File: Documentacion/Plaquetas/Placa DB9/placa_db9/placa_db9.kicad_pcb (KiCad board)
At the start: 2 copper layers, 30 x 16.5 mm, 2 parts, among them J1 Conn_01x09, J2 DB9_Female_MountingHoles

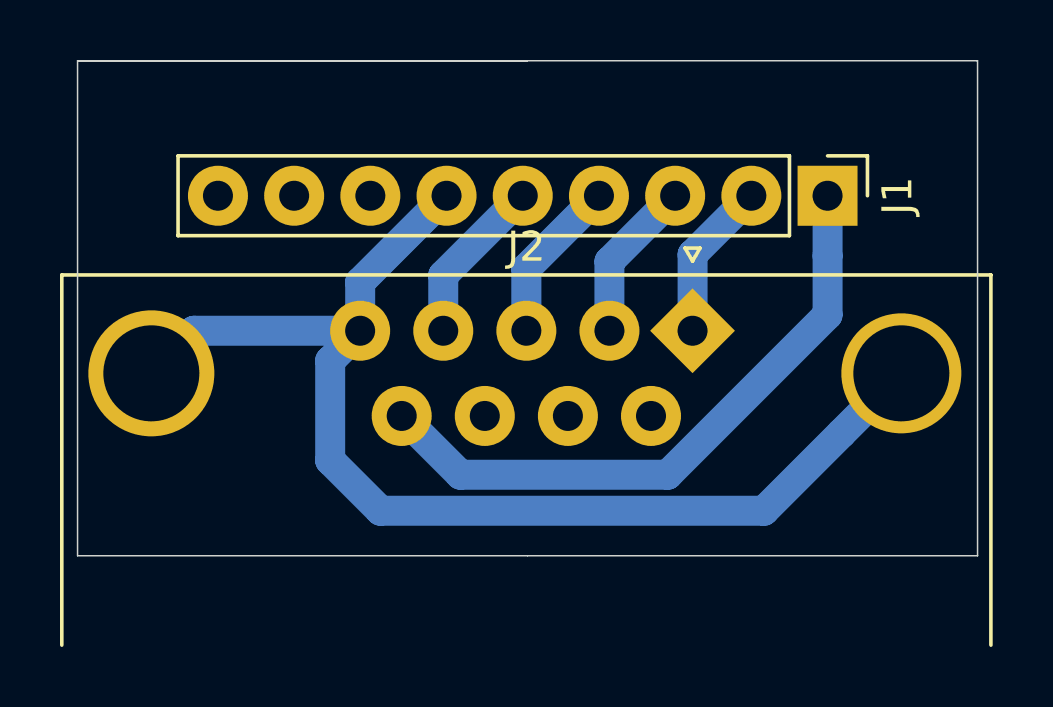
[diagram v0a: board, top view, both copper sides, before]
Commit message: DB9 board with bigger pads
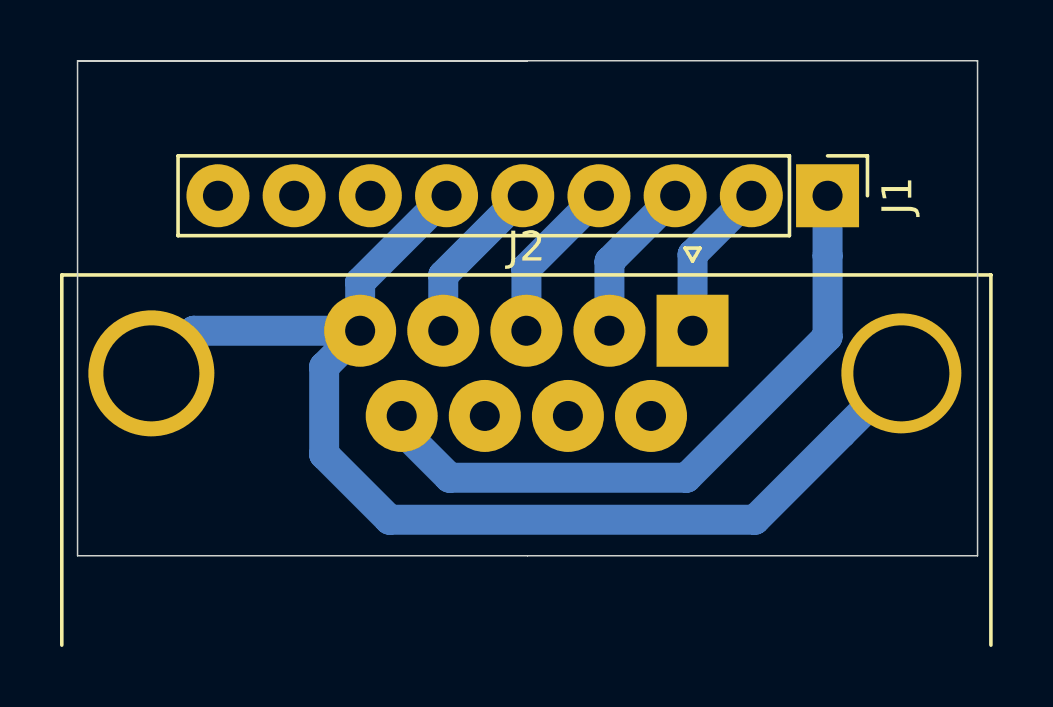
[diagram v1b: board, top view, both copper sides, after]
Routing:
- net /fan_1: track 21.2 -> 22.0 mm
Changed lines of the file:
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@@
     (thickness 1.6)
     (drawings 14)
-    (tracks 23)
+    (tracks 24)
     (zones 0)
     (modules 2)
@@
   )
   (setup
-    (last_trace_width 0.25)
+    (last_trace_width 1)
     (user_trace_width 0.7)
     (user_trace_width 1)
@@
     (descr "Through hole straight pin header, 1x09, 2.54mm pitch, single row")
     (tags "Through hole pin header THT 1x09 2.54mm single row")
-    (fp_text reference J1 (at 0 -2.33 270) (layer F.SilkS)
+    (fp_text reference J1 (at 0 -2.33 90) (layer F.SilkS)
       (effects (font (size 1 1) (thickness 0.15)))
     )
@@
       (effects (font (size 1 1) (thickness 0.15)))
     )
-    (pad 1 thru_hole rect (at 0 0 270) (size 2 2) (drill 1) (layers *.Cu *.Mask)
+    (pad 1 thru_hole rect (at 0 0 270) (size 2.1 2.1) (drill 1) (layers *.Cu *.Mask)
       (net 7 /fan_1))
-    (pad 2 thru_hole oval (at 0 2.54 270) (size 2 2) (drill 1) (layers *.Cu *.Mask)
+    (pad 2 thru_hole circle (at 0 2.54 270) (size 2.1 2.1) (drill 1) (layers *.Cu *.Mask)
       (net 8 /term_pelt_1))
-    (pad 3 thru_hole circle (at 0 5.08 270) (size 2 2) (drill 1) (layers *.Cu *.Mask)
+    (pad 3 thru_hole circle (at 0 5.08 270) (size 2.1 2.1) (drill 1) (layers *.Cu *.Mask)
       (net 9 /term_pelt_2))
-    (pad 4 thru_hole circle (at 0 7.62 270) (size 2 2) (drill 1) (layers *.Cu *.Mask)
+    (pad 4 thru_hole circle (at 0 7.62 270) (size 2.1 2.1) (drill 1) (layers *.Cu *.Mask)
       (net 10 /term_disip_1))
-    (pad 5 thru_hole circle (at 0 10.16 270) (size 2 2) (drill 1) (layers *.Cu *.Mask)
+    (pad 5 thru_hole circle (at 0 10.16 270) (size 2.1 2.1) (drill 1) (layers *.Cu *.Mask)
       (net 11 /term_disip_2))
-    (pad 6 thru_hole circle (at 0 12.7 270) (size 2 2) (drill 1) (layers *.Cu *.Mask)
+    (pad 6 thru_hole circle (at 0 12.7 270) (size 2.1 2.1) (drill 1) (layers *.Cu *.Mask)
       (net 12 /fan_2))
-    (pad 7 thru_hole circle (at 0 15.24 270) (size 2 2) (drill 1) (layers *.Cu *.Mask)
+    (pad 7 thru_hole circle (at 0 15.24 270) (size 2.1 2.1) (drill 1) (layers *.Cu *.Mask)
       (net 1 "Net-(J1-Pad7)"))
-    (pad 8 thru_hole circle (at 0 17.78 270) (size 2 2) (drill 1) (layers *.Cu *.Mask)
+    (pad 8 thru_hole circle (at 0 17.78 270) (size 2.1 2.1) (drill 1) (layers *.Cu *.Mask)
       (net 2 "Net-(J1-Pad8)"))
-    (pad 9 thru_hole circle (at 0 20.32 270) (size 2 2) (drill 1) (layers *.Cu *.Mask)
+    (pad 9 thru_hole circle (at 0 20.32 270) (size 2.1 2.1) (drill 1) (layers *.Cu *.Mask)
       (net 3 "Net-(J1-Pad9)"))
     (model ${KISYS3DMOD}/Connector_PinHeader_2.54mm.3dshapes/PinHeader_1x09_P2.54mm_Vertical.wrl
@@
       (effects (font (size 1 1) (thickness 0.15)))
     )
-    (pad 1 thru_hole rect (at 0 0 45) (size 2 2) (drill 1) (layers *.Cu *.Mask)
+    (pad 1 thru_hole rect (at 0 0) (size 2.4 2.4) (drill 1) (layers *.Cu *.Mask)
       (net 8 /term_pelt_1))
-    (pad 2 thru_hole circle (at -2.77 0) (size 2 2) (drill 1) (layers *.Cu *.Mask)
+    (pad 2 thru_hole circle (at -2.77 0) (size 2.4 2.4) (drill 1) (layers *.Cu *.Mask)
       (net 9 /term_pelt_2))
-    (pad 3 thru_hole circle (at -5.54 0) (size 2 2) (drill 1) (layers *.Cu *.Mask)
+    (pad 3 thru_hole circle (at -5.54 0) (size 2.4 2.4) (drill 1) (layers *.Cu *.Mask)
       (net 10 /term_disip_1))
-    (pad 4 thru_hole circle (at -8.31 0) (size 2 2) (drill 1) (layers *.Cu *.Mask)
+    (pad 4 thru_hole circle (at -8.31 0) (size 2.4 2.4) (drill 1) (layers *.Cu *.Mask)
       (net 11 /term_disip_2))
-    (pad 5 thru_hole circle (at -11.08 0) (size 2 2) (drill 1) (layers *.Cu *.Mask)
+    (pad 5 thru_hole circle (at -11.08 0) (size 2.4 2.4) (drill 1) (layers *.Cu *.Mask)
       (net 12 /fan_2))
-    (pad 6 thru_hole circle (at -1.385 2.84) (size 2 2) (drill 1) (layers *.Cu *.Mask)
+    (pad 6 thru_hole circle (at -1.385 2.84) (size 2.4 2.4) (drill 1) (layers *.Cu *.Mask)
       (net 4 "Net-(J2-Pad6)"))
-    (pad 7 thru_hole circle (at -4.155 2.84) (size 2 2) (drill 1) (layers *.Cu *.Mask)
+    (pad 7 thru_hole circle (at -4.155 2.84) (size 2.4 2.4) (drill 1) (layers *.Cu *.Mask)
       (net 5 "Net-(J2-Pad7)"))
-    (pad 8 thru_hole circle (at -6.925 2.84) (size 2 2) (drill 1) (layers *.Cu *.Mask)
+    (pad 8 thru_hole circle (at -6.925 2.84) (size 2.4 2.4) (drill 1) (layers *.Cu *.Mask)
       (net 6 "Net-(J2-Pad8)"))
-    (pad 9 thru_hole circle (at -9.695 2.84) (size 2 2) (drill 1) (layers *.Cu *.Mask)
+    (pad 9 thru_hole circle (at -9.695 2.84) (size 2.4 2.4) (drill 1) (layers *.Cu *.Mask)
       (net 7 /fan_1))
     (pad 0 thru_hole circle (at -18.04 1.42) (size 4.2 4.2) (drill 3.2) (layers *.Cu *.Mask)
@@
   (gr_line (start 15 15) (end 30 15) (layer Edge.Cuts) (width 0.05))
   (segment (start 40 21.5) (end 40 19.5) (width 1) (layer B.Cu) (net 7))
-  (segment (start 34.671002 28.8) (end 40 23.471002) (width 1) (layer B.Cu) (net 7))
-  (segment (start 27.765 28.8) (end 34.671002 28.8) (width 1) (layer B.Cu) (net 7))
-  (segment (start 40 23.471002) (end 40 21.5) (width 1) (layer B.Cu) (net 7))
-  (segment (start 25.805 26.84) (end 27.765 28.8) (width 1) (layer B.Cu) (net 7))
+  (segment (start 40 24.2) (end 40 21.5) (width 1) (layer B.Cu) (net 7))
+  (segment (start 35.3 28.9) (end 40 24.2) (width 1) (layer B.Cu) (net 7))
+  (segment (start 27.4 28.9) (end 35.3 28.9) (width 1) (layer B.Cu) (net 7))
+  (segment (start 25.805 26.84) (end 25.805 27.305) (width 1) (layer B.Cu) (net 7))
+  (segment (start 25.805 27.305) (end 27.4 28.9) (width 1) (layer B.Cu) (net 7))
   (segment (start 35.5 21.46) (end 37.46 19.5) (width 1) (layer B.Cu) (net 8))
   (segment (start 35.5 24) (end 35.5 21.46) (width 1) (layer B.Cu) (net 8))
@@
   (segment (start 18.88 24) (end 17.46 25.42) (width 1) (layer B.Cu) (net 12))
   (segment (start 24.42 24) (end 18.88 24) (width 1) (layer B.Cu) (net 12))
-  (segment (start 25.100011 30.000011) (end 37.879989 30.000011) (width 1) (layer B.Cu) (net 12))
-  (segment (start 37.879989 30.000011) (end 40.460001 27.419999) (width 1) (layer B.Cu) (net 12))
-  (segment (start 23.420001 28.320001) (end 25.100011 30.000011) (width 1) (layer B.Cu) (net 12))
-  (segment (start 23.420001 24.999999) (end 23.420001 28.320001) (width 1) (layer B.Cu) (net 12))
   (segment (start 40.460001 27.419999) (end 42.46 25.42) (width 1) (layer B.Cu) (net 12))
-  (segment (start 24.42 24) (end 23.420001 24.999999) (width 1) (layer B.Cu) (net 12))
+  (segment (start 37.58 30.3) (end 40.460001 27.419999) (width 1) (layer B.Cu) (net 12))
+  (segment (start 25.4 30.3) (end 37.58 30.3) (width 1) (layer B.Cu) (net 12))
+  (segment (start 23.220001 28.120001) (end 25.4 30.3) (width 1) (layer B.Cu) (net 12))
+  (segment (start 24.42 24) (end 23.220001 25.199999) (width 1) (layer B.Cu) (net 12))
+  (segment (start 23.220001 25.199999) (end 23.220001 28.120001) (width 1) (layer B.Cu) (net 12))
 )
